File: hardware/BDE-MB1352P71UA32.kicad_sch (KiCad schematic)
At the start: 10 parts, among them J22 Conn_ARM_JTAG_SWD_10, SW1 SW_Push, U1 USBLC6-2P6, U23 BDE-MB1352P71UA32, U3 USBLC6-2P6

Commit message: usbc-update
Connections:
- no-connect marks 20 -> 21
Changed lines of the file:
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@@
+	)
+	(no_connect
+		(at 144.78 127)
 	)
 	(no_connect

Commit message: Debugging LED added
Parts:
- R7: footprint Resistor_SMD:R_0603_1608Metric -> Resistor_SMD:R_0805_2012Metric
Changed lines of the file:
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@@
 			)
 		)
-		(property "Footprint" "Resistor_SMD:R_0603_1608Metric"
+		(property "Footprint" "Resistor_SMD:R_0805_2012Metric"
 			(at 136.652 77.47 90)
 			(effects

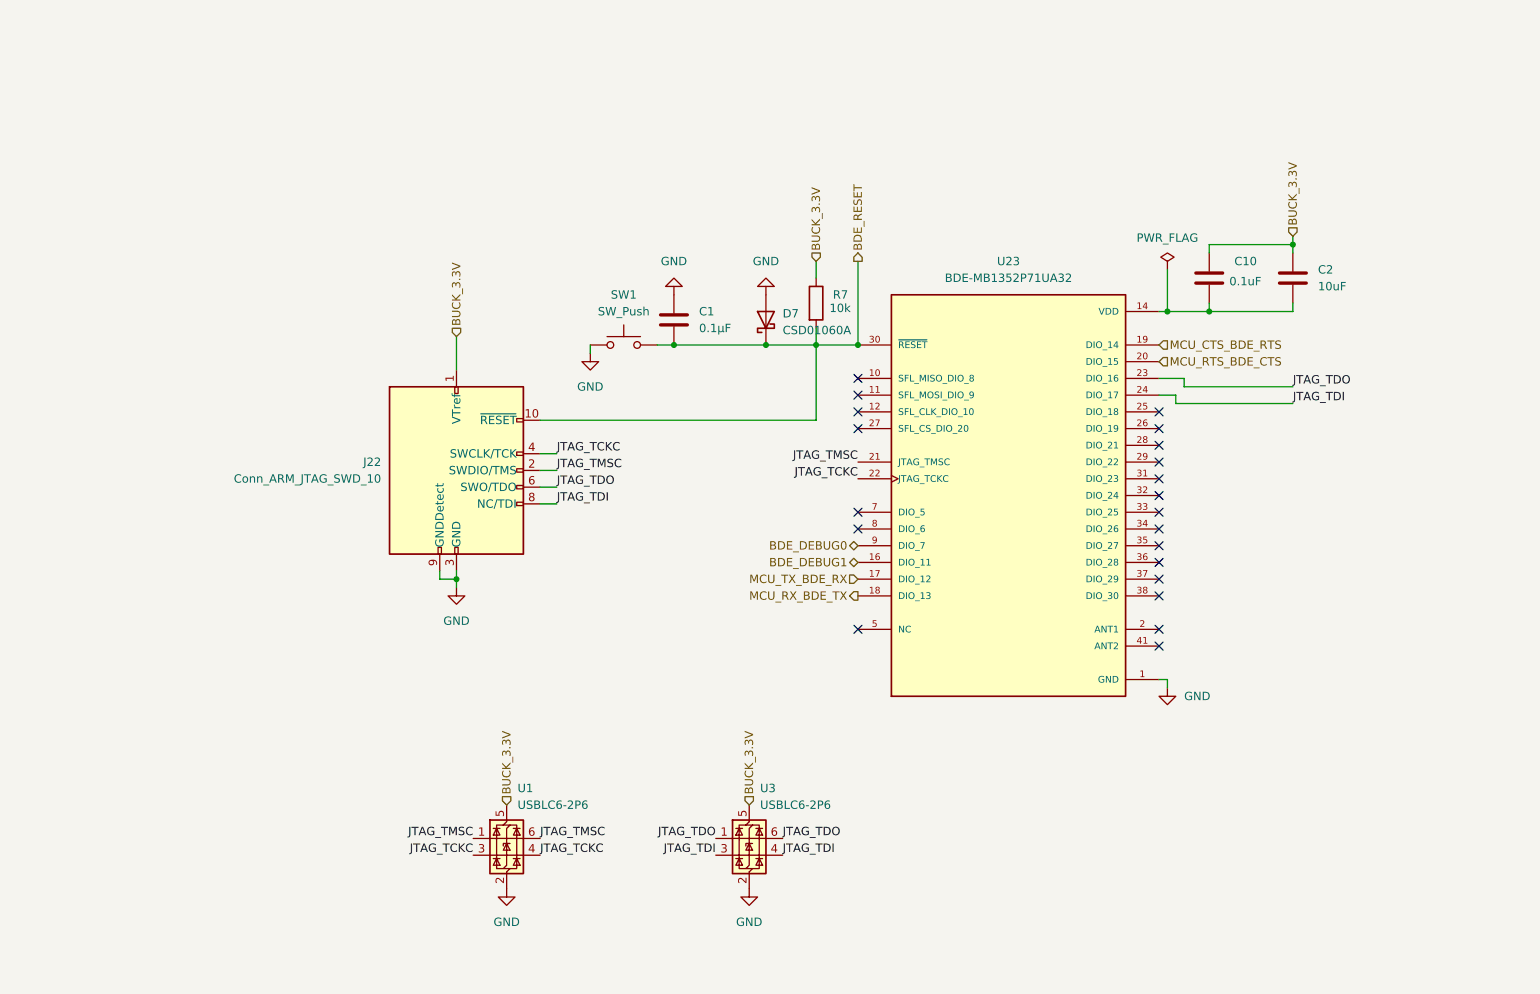
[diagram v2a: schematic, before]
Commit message: Fixed MCU JTAG/Reordered pages
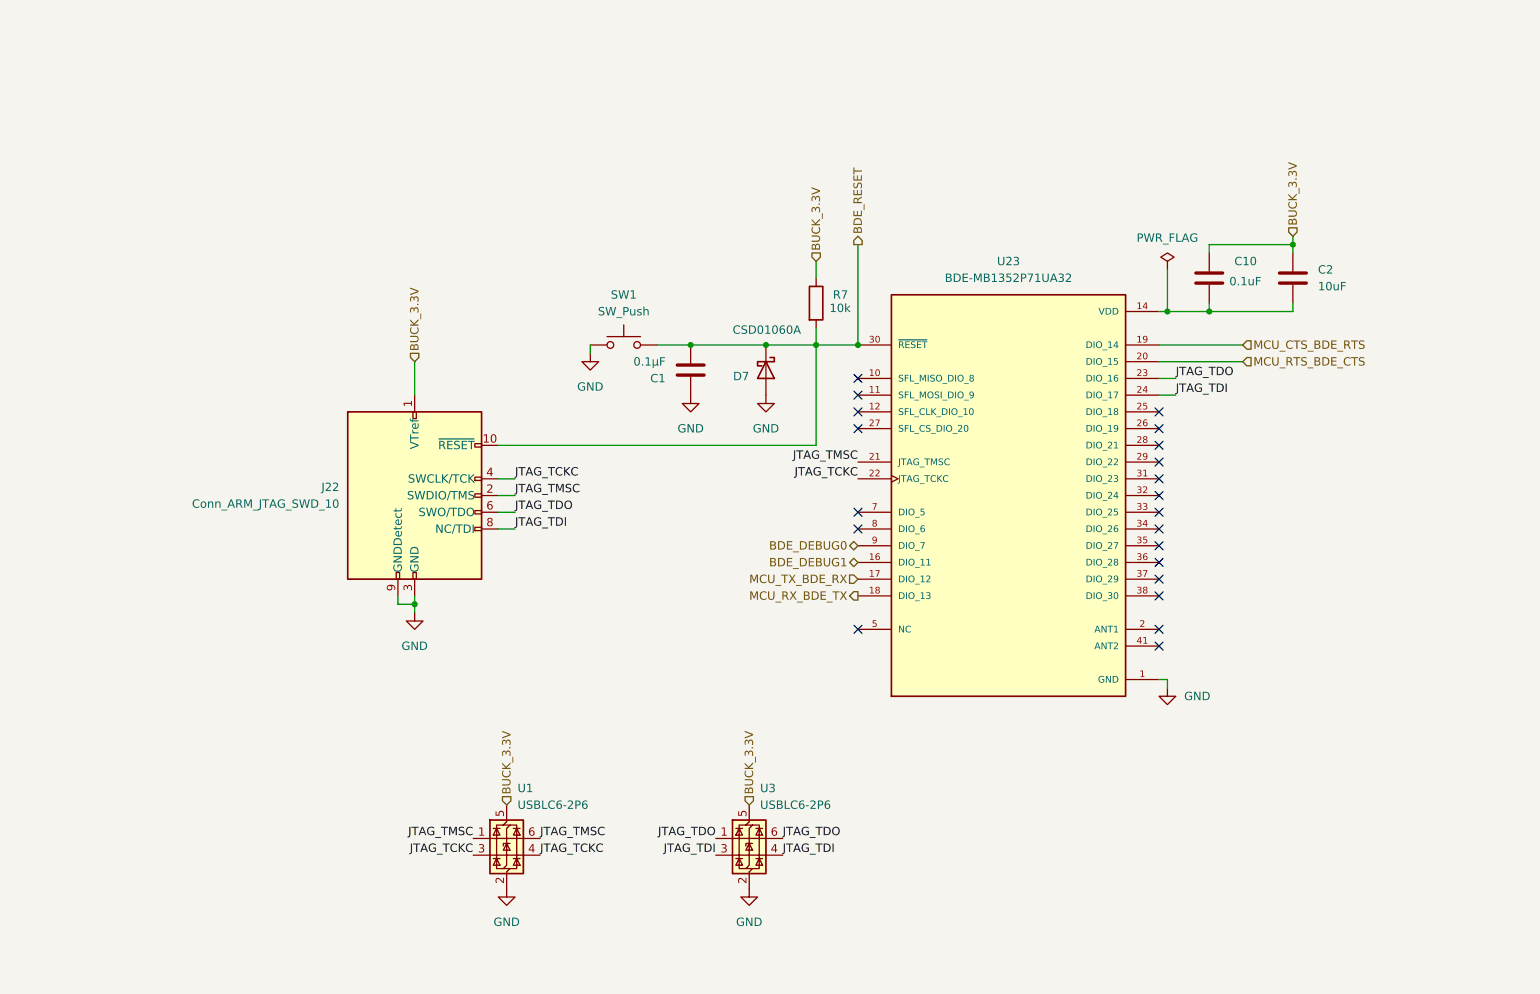
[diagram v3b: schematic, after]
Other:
- moved on the sheet: C1, D7, J22

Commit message: BDE JTAG pullup
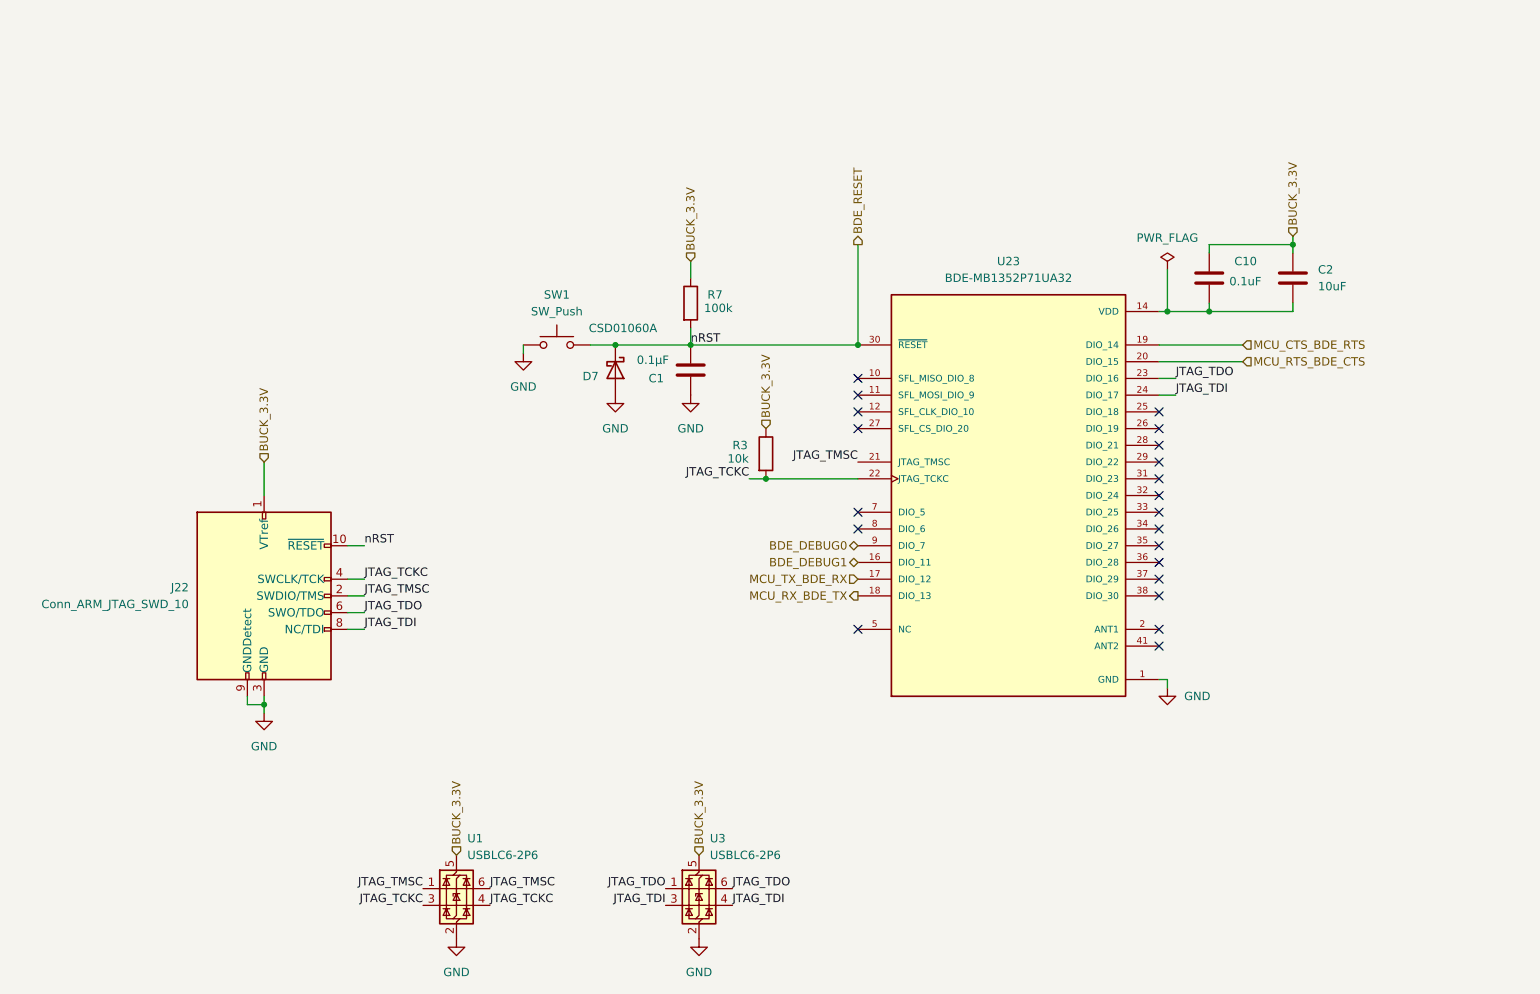
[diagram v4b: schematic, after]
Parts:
- added R3: 10k, Resistor_SMD:R_0805_2012Metric, symbol Device:R
- R7: value 10k -> 100k
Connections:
- net BUCK_3.3V: now also R3.1
- net JTAG_TCKC: now also R3.2
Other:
- moved on the sheet: D7, J22, R7, SW1, U1, U3

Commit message: cleanup
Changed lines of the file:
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@@
 	(wire
 		(pts
-			(xy 128.27 104.14) (xy 130.81 104.14)
+			(xy 123.19 104.14) (xy 130.81 104.14)
 		)
 		(stroke
@@
 	)
 	(label "JTAG_TCKC"
-		(at 128.27 104.14 180)
+		(at 123.19 104.14 180)
 		(effects
 			(font
@@
 		)
 	)
-	(label "nRST"
-		(at 119.38 83.82 0)
-		(effects
-			(font
-				(size 1.27 1.27)
-			)
-			(justify left bottom)
-		)
-	)
 	(label "JTAG_TDO"
 		(at 125.73 166.37 0)
@@
 	(label "JTAG_TDI"
 		(at 125.73 168.91 0)
-		(effects
-			(font
-				(size 1.27 1.27)
-			)
-			(justify left bottom)
-		)
-	)
-	(label "nRST"
-		(at 69.85 114.3 0)
 		(effects
 			(font
@@
 		(effects
 			(font
+				(size 1.27 1.27)
+			)
+			(justify left)
+		)
+	)
+	(hierarchical_label "BDE_RESET"
+		(shape input)
+		(at 69.85 114.3 0)
+		(effects
+			(font

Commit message: Replaced 3.3V symbol
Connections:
- net BUCK_3.3V renamed +3.3V

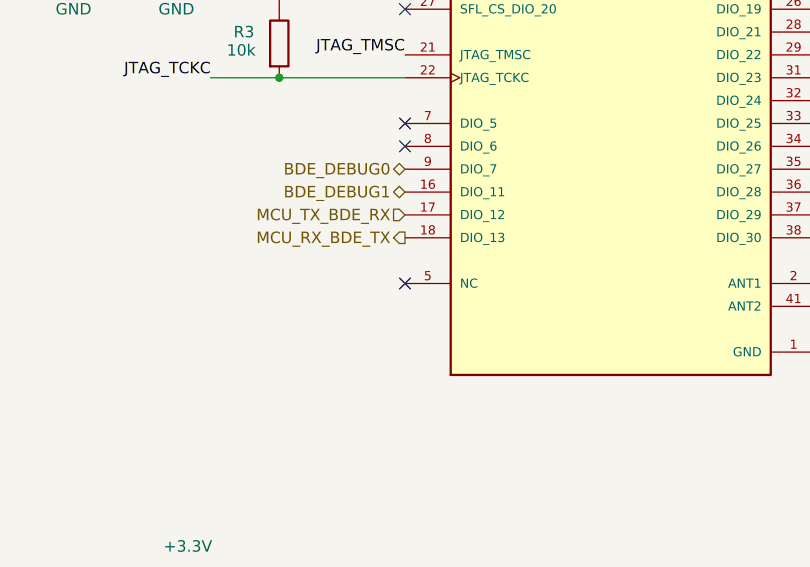
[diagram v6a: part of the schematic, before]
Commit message: updated major symbol and footprints
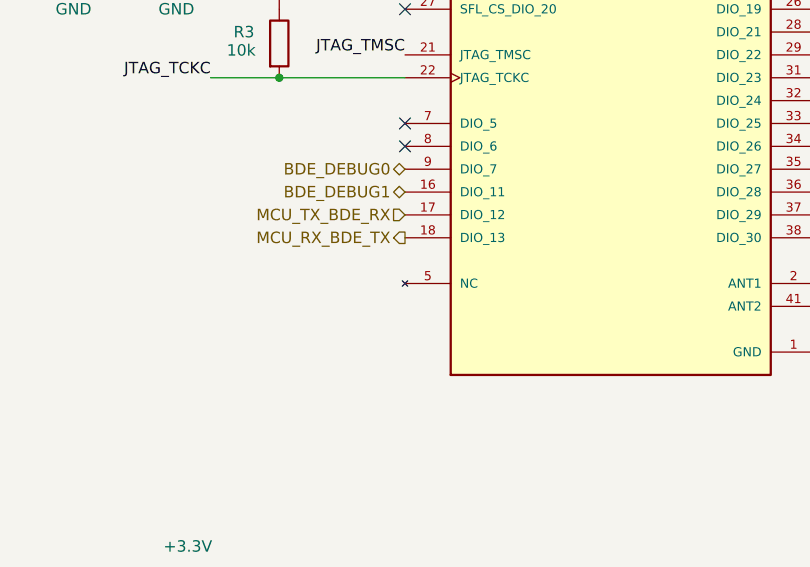
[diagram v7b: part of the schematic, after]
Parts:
- U23: footprint Custom_Parts:XCVR_BDE-MB1352P71UA32 -> pyronet_footprints:XCVR_BDE-MB1352P71UA32; symbol BDE-MB1352P71UA32:BDE-MB1352P71UA32 -> pyronet_symbols:BDE-MB1352P71UA32
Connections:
- no-connect marks 21 -> 20
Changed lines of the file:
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@@
-	)
-	(no_connect
-		(at 144.78 127)
 	)
 	(no_connect
@@
 	)
 	(symbol
-		(lib_id "BDE-MB1352P71UA32:BDE-MB1352P71UA32")
+		(lib_id "pyronet_symbols:BDE-MB1352P71UA32")
 		(at 167.64 106.68 0)
 		(unit 1)
@@
 			)
 		)
-		(property "Footprint" "Custom_Parts:XCVR_BDE-MB1352P71UA32"
+		(property "Footprint" "pyronet_footprints:XCVR_BDE-MB1352P71UA32"
 			(at 167.64 106.68 0)
 			(effects

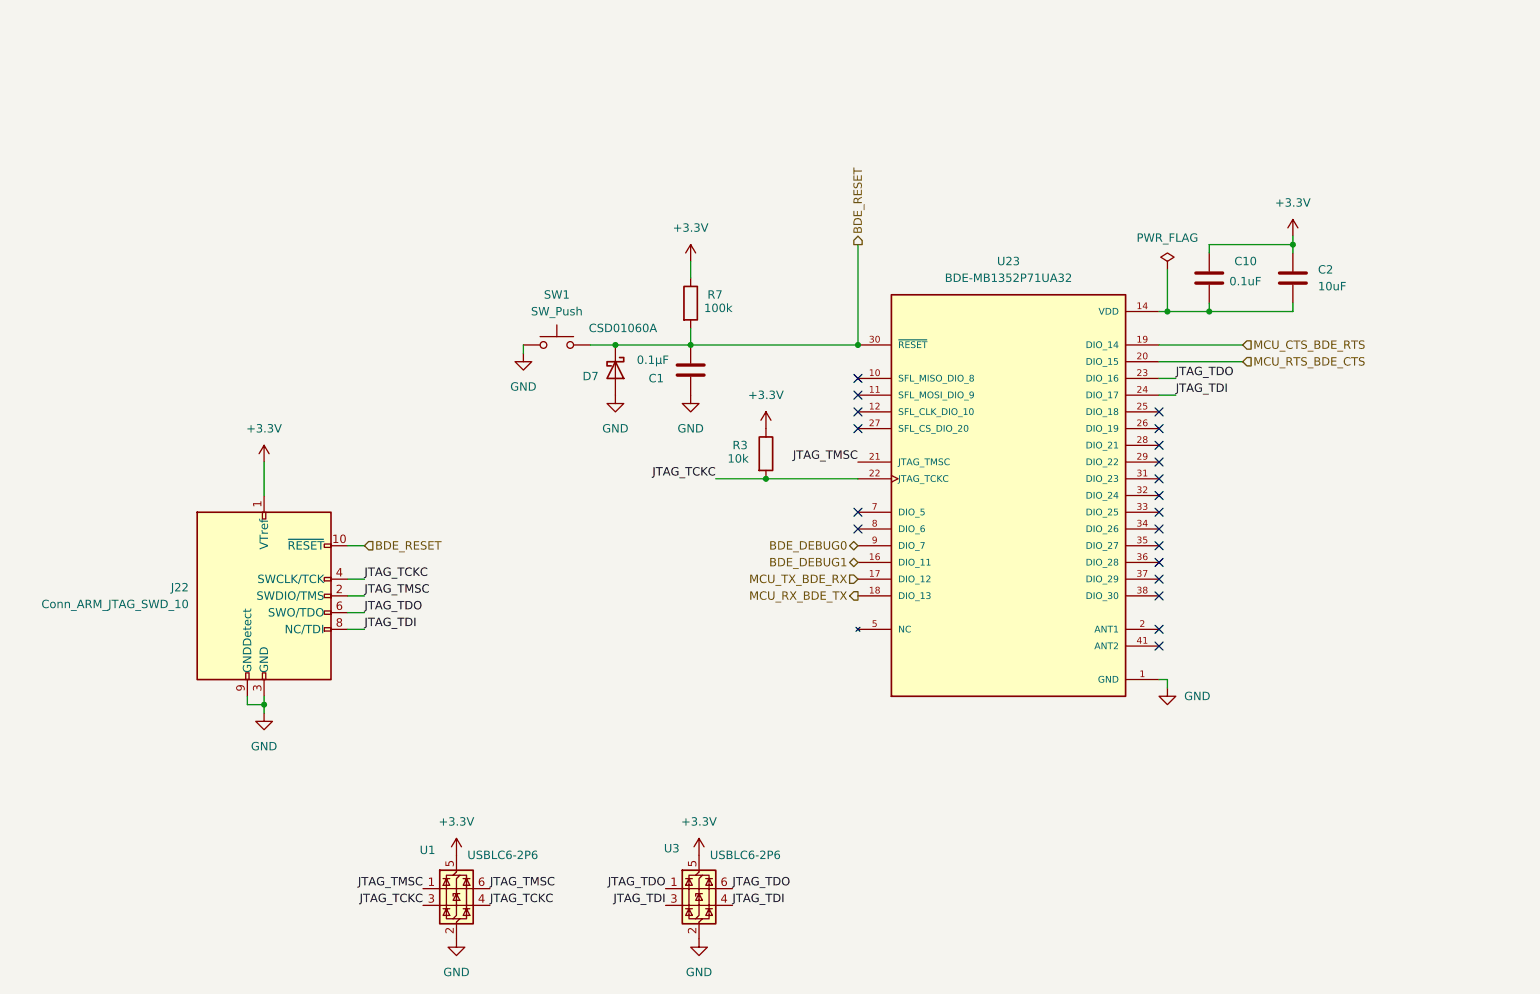
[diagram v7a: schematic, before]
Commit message: updated 5V power and pin
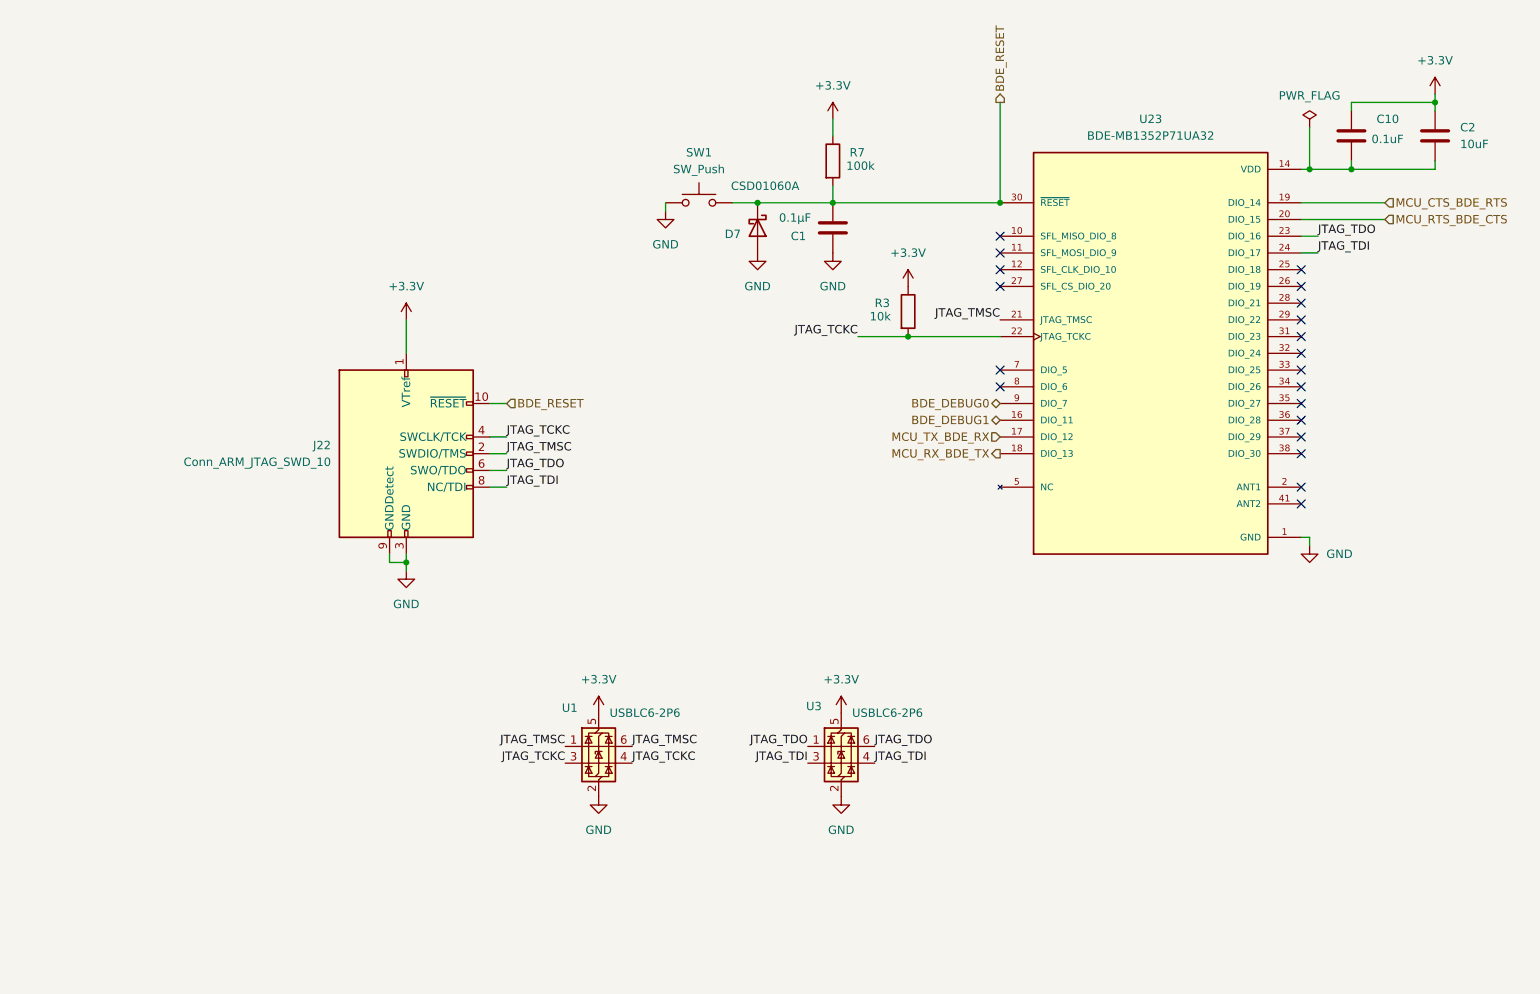
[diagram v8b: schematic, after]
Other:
- moved on the sheet: C1, C10, C2, D7, J22, R3, R7, SW1, U1, U23, U3
